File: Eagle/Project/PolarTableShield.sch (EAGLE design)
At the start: 42 parts, among them IC2 LM358D, J1 Pi Power Jack, J10 LED + Radio, J2 Header - Right angled, female, J3 Pi Connection, J5 IR Sensors, J6 Switch A + B, J7 Switch C + D, J8 Switch E + F, Q1 BC337, Q2 2N3906, Q3 BC547, Q4 2N7000, Q5 2N7000, U3 SN74HC595DR

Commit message: Layout and added frame.
Added status lights.
Matched trace lengths on the I2C bus.
Added logo.
Fixed up I2C connection on the SX1509 pins.
Added better labels and descriptions.
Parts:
- added LED1, LED2: (no value), led:LEDCHIP-LED0805
- added R13, R14: 1k, rcl:R-EU_M0805
- B1: value Connect down to Arduino -> ARDUINO_UNO_R3_SHIELDNOLABELS
- B2: value Connect up to motor shield -> ARDUINO_UNO_R3_SHIELDNOLABELS
- JP2: value Bypass Power Control -> JUMPER-SMT_2_NO_SILK
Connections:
- new net N$10: LED2.A, R14.2
- new net N$9: LED1.C, R13.1
- net !INT: now also U$1G$1.!INT; no longer U$1G$1.!RST
- net !RES: now also U$1G$1.!RST
- net 5V: now also R14.1
- net 5V_SUPPLY: now also LED1.A
- net N$6: now also R13.2
- net SCL_5V: now also LED2.C
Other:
- note added: "External 12V to 5V Buck Converter"
- note added: "Extra I2C"
- note added: "Extras"
- note added: "GPIO Expansions"
- note added: "Hard reset on button hold (5s)"
- note added: "Headers"
- note added: "Headers down to Arduino"
- note added: "Headers to Motor Shield"
- note added: "Logic Level Converter"
- note added: "Open JP3 to disable hard reset."
- note added: "Output to Raspberry Pi"
- note added: "PI Connection"
- note added: "SX1509 Headers for breakout board NOTE: 3.3V"
- note added: "Shift Register for motor settings NOTE: 5V"
- note added: "Short JP2 to disable control of Pi Power from Arduino"
- note removed: "GPIO Expander"
- note removed: "Long Press Detection (5s)"
- note removed: "PI"
- note removed: "Shift Register for motor settings"
- note removed: "Start the timer when the signal grounds"
- moved on the sheet: B1, B2, C1, C2, C4, C5, C9, D1, IC2A, J1, J10, J2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

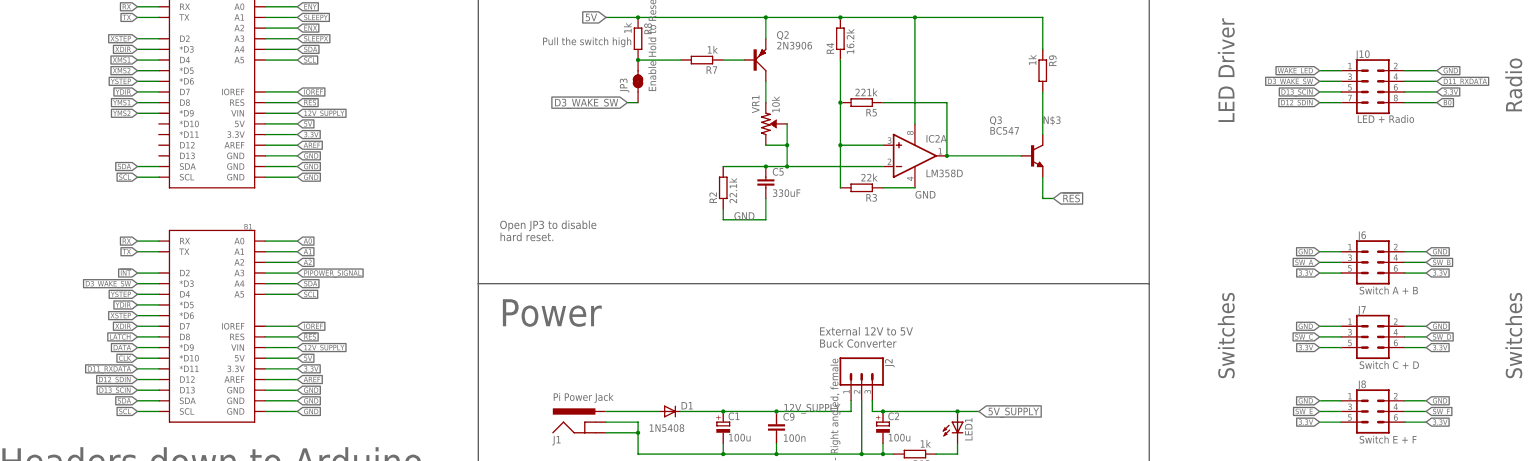
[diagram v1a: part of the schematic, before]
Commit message: Moved the LED drive connection onto hardware SPI pins.
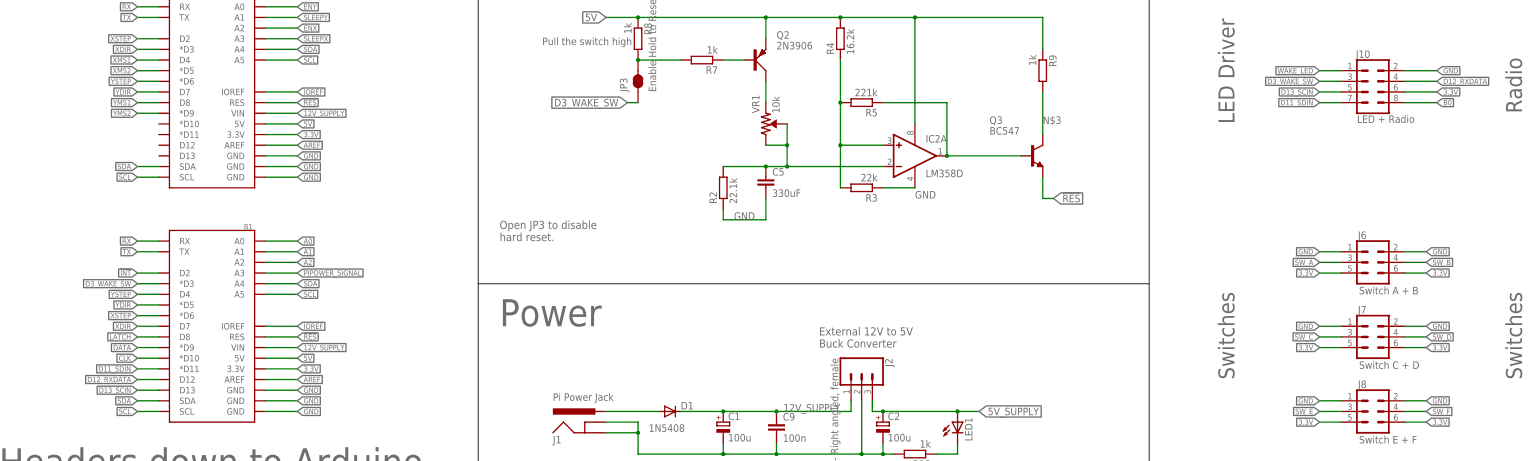
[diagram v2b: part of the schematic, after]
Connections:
- removed net D11_RXDATA: B1.*D11, J10.4
- removed net D12_SDIN: B1.D12, J10.7
- new net D11_SDIN: B1.*D11, J10.7
- new net D12_RXDATA: B1.D12, J10.4
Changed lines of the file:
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@@
 </segment>
 </net>
-<net name="D11_RXDATA" class="4">
-<segment>
-<pinref part="B1" gate="G$1" pin="*D11"/>
-<wire x1="45.72" y1="147.32" x2="40.64" y2="147.32" width="0.1524" layer="91"/>
-<label x="40.64" y="147.32" size="1.27" layer="95" rot="MR0" xref="yes"/>
-</segment>
+<net name="D12_RXDATA" class="4">
 <segment>
 <wire x1="342.9" y1="215.9" x2="350.52" y2="215.9" width="0.1524" layer="91"/>
@@
 <pinref part="J10" gate="G$1" pin="4"/>
 </segment>
-</net>
-<net name="D12_SDIN" class="4">
 <segment>
 <pinref part="B1" gate="G$1" pin="D12"/>
 <wire x1="45.72" y1="144.78" x2="40.64" y2="144.78" width="0.1524" layer="91"/>
 <label x="40.64" y="144.78" size="1.27" layer="95" rot="MR0" xref="yes"/>
-</segment>
-<segment>
-<wire x1="327.66" y1="210.82" x2="322.58" y2="210.82" width="0.1524" layer="91"/>
-<label x="322.58" y="210.82" size="1.27" layer="95" rot="MR0" xref="yes"/>
-<pinref part="J10" gate="G$1" pin="7"/>
 </segment>
 </net>
@@
 </segment>
 </net>
+<net name="D11_SDIN" class="0">
+<segment>
+<pinref part="B1" gate="G$1" pin="*D11"/>
+<wire x1="45.72" y1="147.32" x2="40.64" y2="147.32" width="0.1524" layer="91"/>
+<label x="40.64" y="147.32" size="1.27" layer="95" rot="MR0" xref="yes"/>
+</segment>
+<segment>
+<wire x1="327.66" y1="210.82" x2="322.58" y2="210.82" width="0.1524" layer="91"/>
+<label x="322.58" y="210.82" size="1.27" layer="95" rot="MR0" xref="yes"/>
+<pinref part="J10" gate="G$1" pin="7"/>
+</segment>
+</net>

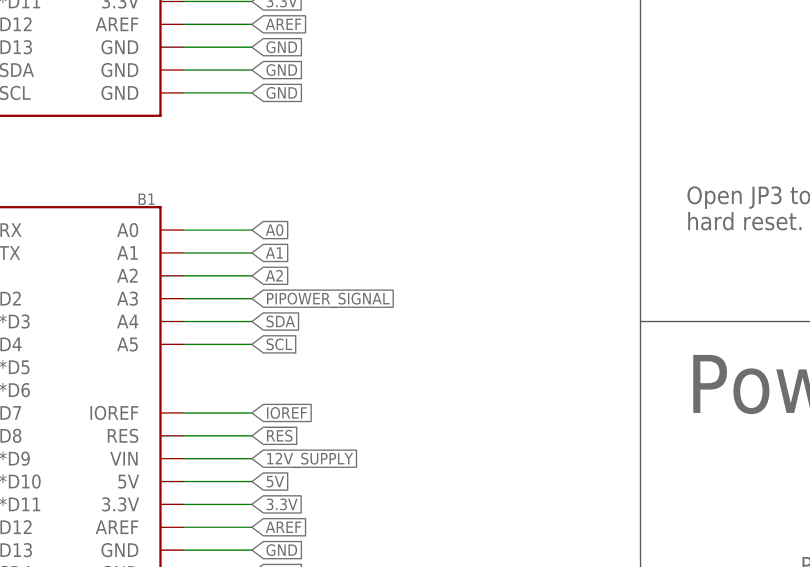
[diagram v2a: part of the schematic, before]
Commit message: Added a LED for error signals
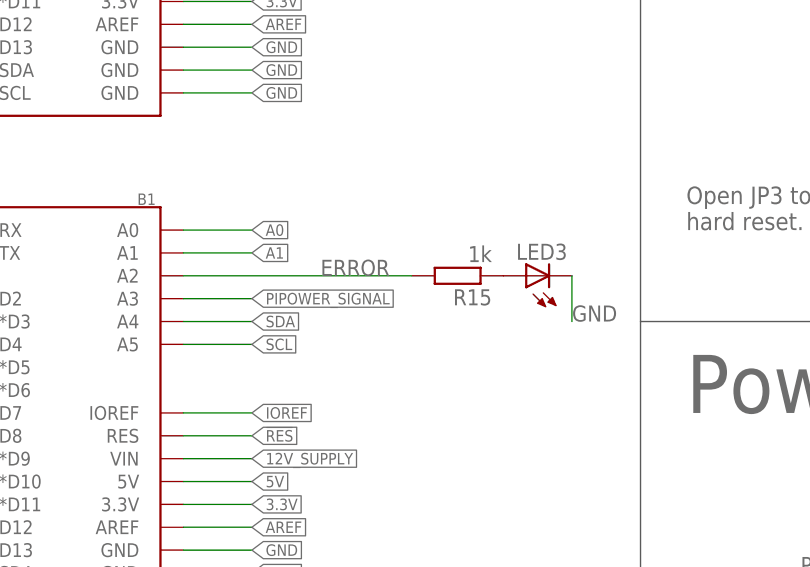
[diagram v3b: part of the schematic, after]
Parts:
- added LED3: (no value), led:LEDCHIP-LED0805
- added R15: 1k, rcl:R-EU_M0805
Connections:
- new net ERROR: B1.A2, R15.2
- new net N$11: LED3.A, R15.1
- net A2: no longer B1.A2
- net GND: now also LED3.C
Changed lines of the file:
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@@
 <part name="LED2" library="led" library_urn="urn:adsk.eagle:library:259" deviceset="LED" device="CHIP-LED0805" package3d_urn="urn:adsk.eagle:package:15818/2"/>
 <part name="R14" library="rcl" library_urn="urn:adsk.eagle:library:334" deviceset="R-EU_" device="M0805" package3d_urn="urn:adsk.eagle:package:23556/1" value="1k"/>
+<part name="LED3" library="led" library_urn="urn:adsk.eagle:library:259" deviceset="LED" device="CHIP-LED0805" package3d_urn="urn:adsk.eagle:package:15818/2"/>
+<part name="R15" library="rcl" library_urn="urn:adsk.eagle:library:334" deviceset="R-EU_" device="M0805" package3d_urn="urn:adsk.eagle:package:23556/1" value="1k"/>
 </parts>
 <sheets>
@@
 <attribute name="VALUE" x="237.998" y="41.91" size="1.778" layer="96" rot="R270"/>
 </instance>
+<instance part="LED3" gate="G$1" x="109.22" y="172.72" rot="R90">
+<attribute name="NAME" x="113.792" y="176.276" size="1.778" layer="95" rot="R180"/>
+<attribute name="VALUE" x="113.792" y="178.435" size="1.778" layer="96" rot="R180"/>
+</instance>
+<instance part="R15" gate="G$1" x="101.6" y="172.72" rot="R180">
+<attribute name="NAME" x="105.41" y="171.2214" size="1.778" layer="95" rot="R180"/>
+<attribute name="VALUE" x="105.41" y="176.022" size="1.778" layer="96" rot="R180"/>
+</instance>
 </instances>
 <busses>
@@
 <wire x1="342.9" y1="96.52" x2="347.98" y2="96.52" width="0.1524" layer="91"/>
 <label x="347.98" y="96.52" size="1.27" layer="95" xref="yes"/>
+</segment>
+<segment>
+<pinref part="LED3" gate="G$1" pin="C"/>
+<wire x1="114.3" y1="172.72" x2="114.3" y2="167.64" width="0.1524" layer="91"/>
+<label x="114.3" y="167.64" size="1.778" layer="95"/>
 </segment>
 </net>
@@
 <net name="A2" class="4">
 <segment>
-<pinref part="B1" gate="G$1" pin="A2"/>
-<wire x1="71.12" y1="172.72" x2="78.74" y2="172.72" width="0.1524" layer="91"/>
-<label x="78.74" y="172.72" size="1.27" layer="95" xref="yes"/>
-</segment>
-<segment>
 <pinref part="J5" gate="G$1" pin="6"/>
 <wire x1="342.9" y1="93.98" x2="347.98" y2="93.98" width="0.1524" layer="91"/>
@@
 </segment>
 </net>
+<net name="ERROR" class="0">
+<segment>
+<pinref part="B1" gate="G$1" pin="A2"/>
+<pinref part="R15" gate="G$1" pin="2"/>
+<wire x1="71.12" y1="172.72" x2="96.52" y2="172.72" width="0.1524" layer="91"/>
+<label x="86.36" y="172.72" size="1.778" layer="95"/>
+</segment>
+</net>
+<net name="N$11" class="0">
+<segment>
+<pinref part="R15" gate="G$1" pin="1"/>
+<pinref part="LED3" gate="G$1" pin="A"/>
+</segment>
+</net>

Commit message: Moved the relative encode switches to the Arduino
Added hardware XOR on the relative encode switches.
Combined the main switch and encoder interrupt connections.
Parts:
- removed LED3: (no value), led:LEDCHIP-LED0805
- removed R15: 1k, rcl:R-EU_M0805
- added IC1: 74AHC1G86DBV, 74xx-little-us:74AHC1G86DBV
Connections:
- removed net A0: B1.A0, J5.10
- removed net A1: B1.A1, J5.8
- removed net D3_WAKE_SW: B1.*D3, J10.3, JP3.1
- removed net ERROR: B1.A2, R15.2
- removed net N$11: LED3.A, R15.1
- removed net SW_E: J8.3, U$1G$2.P$4
- removed net SW_F: J8.4, U$1G$2.P$3
- new net A0_SW_E: B1.A0, IC1A.I0, J8.3
- new net A1_SW_F: B1.A1, IC1A.I1, J8.4
- new net A2_WAKE_SW: B1.*D3, B1.A2, IC1A.O, J10.3, JP3.1
- new net B5: J4.7, U$1G$2.P$5
- new net B6: J4.8, U$1G$2.P$6
- net B3: now also J5.8, U$1G$2.P$3; no longer J4.7, U$1G$2.P$5
- net B4: now also J5.10, U$1G$2.P$4; no longer J4.8, U$1G$2.P$6
- net GND: no longer LED3.C
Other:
- note added: "WIP: OR gate for interupts"
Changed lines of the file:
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@@
 <part name="LED2" library="led" library_urn="urn:adsk.eagle:library:259" deviceset="LED" device="CHIP-LED0805" package3d_urn="urn:adsk.eagle:package:15818/2"/>
 <part name="R14" library="rcl" library_urn="urn:adsk.eagle:library:334" deviceset="R-EU_" device="M0805" package3d_urn="urn:adsk.eagle:package:23556/1" value="1k"/>
-<part name="LED3" library="led" library_urn="urn:adsk.eagle:library:259" deviceset="LED" device="CHIP-LED0805" package3d_urn="urn:adsk.eagle:package:15818/2"/>
-<part name="R15" library="rcl" library_urn="urn:adsk.eagle:library:334" deviceset="R-EU_" device="M0805" package3d_urn="urn:adsk.eagle:package:23556/1" value="1k"/>
+<part name="IC1" library="74xx-little-us" library_urn="urn:adsk.eagle:library:87" deviceset="74*1G86" device="DBV" package3d_urn="urn:adsk.eagle:package:2406/1" technology="AHC"/>
 </parts>
 <sheets>
@@
 <text x="127" y="177.8" size="1.9304" layer="95" font="vector">Open JP3 to disable
 hard reset.</text>
+<text x="96.52" y="152.4" size="1.9304" layer="95" font="vector">WIP: OR gate for interupts</text>
 </plain>
 <instances>
@@
 <attribute name="VALUE" x="237.998" y="41.91" size="1.778" layer="96" rot="R270"/>
 </instance>
-<instance part="LED3" gate="G$1" x="109.22" y="172.72" rot="R90">
-<attribute name="NAME" x="113.792" y="176.276" size="1.778" layer="95" rot="R180"/>
-<attribute name="VALUE" x="113.792" y="178.435" size="1.778" layer="96" rot="R180"/>
-</instance>
-<instance part="R15" gate="G$1" x="101.6" y="172.72" rot="R180">
-<attribute name="NAME" x="105.41" y="171.2214" size="1.778" layer="95" rot="R180"/>
-<attribute name="VALUE" x="105.41" y="176.022" size="1.778" layer="96" rot="R180"/>
+<instance part="IC1" gate="A" x="-27.94" y="177.8">
+<attribute name="NAME" x="-35.56" y="183.515" size="1.778" layer="95"/>
+<attribute name="VALUE" x="-35.56" y="170.18" size="1.778" layer="96"/>
 </instance>
 </instances>
@@
 <wire x1="342.9" y1="96.52" x2="347.98" y2="96.52" width="0.1524" layer="91"/>
 <label x="347.98" y="96.52" size="1.27" layer="95" xref="yes"/>
-</segment>
-<segment>
-<pinref part="LED3" gate="G$1" pin="C"/>
-<wire x1="114.3" y1="172.72" x2="114.3" y2="167.64" width="0.1524" layer="91"/>
-<label x="114.3" y="167.64" size="1.778" layer="95"/>
 </segment>
 </net>
@@
 <wire x1="127" y1="30.48" x2="132.08" y2="30.48" width="0.1524" layer="91"/>
 <label x="132.08" y="30.48" size="1.27" layer="95" xref="yes"/>
-</segment>
-</net>
-<net name="SW_E" class="3">
-<segment>
-<pinref part="J8" gate="G$1" pin="3"/>
-<wire x1="327.66" y1="137.16" x2="322.58" y2="137.16" width="0.1524" layer="91"/>
-<label x="322.58" y="137.16" size="1.27" layer="95" rot="MR0" xref="yes"/>
-</segment>
-<segment>
-<pinref part="U$1" gate="G$2" pin="P$4"/>
-<wire x1="86.36" y1="35.56" x2="81.28" y2="35.56" width="0.1524" layer="91"/>
-<label x="81.28" y="35.56" size="1.27" layer="95" rot="R180" xref="yes"/>
-</segment>
-</net>
-<net name="SW_F" class="3">
-<segment>
-<pinref part="J8" gate="G$1" pin="4"/>
-<wire x1="342.9" y1="137.16" x2="347.98" y2="137.16" width="0.1524" layer="91"/>
-<label x="347.98" y="137.16" size="1.27" layer="95" xref="yes"/>
-</segment>
-<segment>
-<pinref part="U$1" gate="G$2" pin="P$3"/>
-<wire x1="86.36" y1="38.1" x2="81.28" y2="38.1" width="0.1524" layer="91"/>
-<label x="81.28" y="38.1" size="1.27" layer="95" rot="R180" xref="yes"/>
 </segment>
 </net>
@@
 </segment>
 </net>
-<net name="D3_WAKE_SW" class="4">
+<net name="A2_WAKE_SW" class="4">
 <segment>
 <label x="322.58" y="215.9" size="1.27" layer="95" rot="MR0" xref="yes"/>
@@
 </segment>
 <segment>
+<label x="78.74" y="172.72" size="1.27" layer="95" rot="MR180" xref="yes"/>
+<pinref part="B1" gate="G$1" pin="A2"/>
+<wire x1="78.74" y1="172.72" x2="71.12" y2="172.72" width="0.1524" layer="91"/>
+</segment>
+<segment>
+<wire x1="-50.8" y1="165.1" x2="-10.16" y2="165.1" width="0.1524" layer="91"/>
+<wire x1="-10.16" y1="165.1" x2="-10.16" y2="175.26" width="0.1524" layer="91"/>
+<label x="-55.88" y="165.1" size="1.778" layer="95"/>
 <pinref part="B1" gate="G$1" pin="*D3"/>
-<wire x1="45.72" y1="167.64" x2="40.64" y2="167.64" width="0.1524" layer="91"/>
-<label x="40.64" y="167.64" size="1.27" layer="95" rot="MR0" xref="yes"/>
+<wire x1="25.4" y1="175.26" x2="25.4" y2="167.64" width="0.1524" layer="91"/>
+<wire x1="25.4" y1="167.64" x2="45.72" y2="167.64" width="0.1524" layer="91"/>
+<pinref part="IC1" gate="A" pin="O"/>
+<wire x1="-15.24" y1="177.8" x2="-10.16" y2="177.8" width="0.1524" layer="91"/>
+<wire x1="25.4" y1="175.26" x2="-10.16" y2="175.26" width="0.1524" layer="91"/>
+<wire x1="-10.16" y1="175.26" x2="-10.16" y2="177.8" width="0.1524" layer="91"/>
+<junction x="-10.16" y="175.26"/>
 </segment>
 </net>
@@
 </segment>
 </net>
-<net name="B4" class="3">
+<net name="B6" class="3">
 <segment>
 <pinref part="U$1" gate="G$2" pin="P$6"/>
@@
 </segment>
 </net>
-<net name="B3" class="3">
+<net name="B5" class="3">
 <segment>
 <pinref part="U$1" gate="G$2" pin="P$5"/>
@@
 </segment>
 </net>
-<net name="A0" class="4">
+<net name="A0_SW_E" class="4">
 <segment>
 <pinref part="B1" gate="G$1" pin="A0"/>
@@
 </segment>
 <segment>
-<pinref part="J5" gate="G$1" pin="10"/>
-<wire x1="342.9" y1="88.9" x2="347.98" y2="88.9" width="0.1524" layer="91"/>
-<label x="347.98" y="88.9" size="1.27" layer="95" xref="yes"/>
-</segment>
-</net>
-<net name="A1" class="4">
+<pinref part="J8" gate="G$1" pin="3"/>
+<wire x1="327.66" y1="137.16" x2="322.58" y2="137.16" width="0.1524" layer="91"/>
+<label x="322.58" y="137.16" size="1.27" layer="95" rot="MR0" xref="yes"/>
+</segment>
+<segment>
+<pinref part="IC1" gate="A" pin="I0"/>
+<wire x1="-40.64" y1="180.34" x2="-50.8" y2="180.34" width="0.1524" layer="91"/>
+<label x="-55.88" y="180.34" size="1.778" layer="95"/>
+</segment>
+</net>
+<net name="A1_SW_F" class="4">
 <segment>
 <pinref part="B1" gate="G$1" pin="A1"/>
@@
 </segment>
 <segment>
-<pinref part="J5" gate="G$1" pin="8"/>
-<wire x1="342.9" y1="91.44" x2="347.98" y2="91.44" width="0.1524" layer="91"/>
-<label x="347.98" y="91.44" size="1.27" layer="95" xref="yes"/>
+<pinref part="J8" gate="G$1" pin="4"/>
+<wire x1="342.9" y1="137.16" x2="347.98" y2="137.16" width="0.1524" layer="91"/>
+<label x="347.98" y="137.16" size="1.27" layer="95" xref="yes"/>
+</segment>
+<segment>
+<pinref part="IC1" gate="A" pin="I1"/>
+<wire x1="-40.64" y1="175.26" x2="-50.8" y2="175.26" width="0.1524" layer="91"/>
+<label x="-55.88" y="175.26" size="1.778" layer="95"/>
 </segment>
 </net>
@@
 </segment>
 </net>
-<net name="ERROR" class="0">
-<segment>
-<pinref part="B1" gate="G$1" pin="A2"/>
-<pinref part="R15" gate="G$1" pin="2"/>
-<wire x1="71.12" y1="172.72" x2="96.52" y2="172.72" width="0.1524" layer="91"/>
-<label x="86.36" y="172.72" size="1.778" layer="95"/>
-</segment>
-</net>
-<net name="N$11" class="0">
-<segment>
-<pinref part="R15" gate="G$1" pin="1"/>
-<pinref part="LED3" gate="G$1" pin="A"/>
-</segment>
-</net>
+<net name="B3" class="4">
+<segment>
+<pinref part="U$1" gate="G$2" pin="P$3"/>
+<wire x1="86.36" y1="38.1" x2="81.28" y2="38.1" width="0.1524" layer="91"/>
+<label x="81.28" y="38.1" size="1.27" layer="95" rot="R180" xref="yes"/>
+</segment>
+<segment>
+<pinref part="J5" gate="G$1" pin="8"/>
+<wire x1="342.9" y1="91.44" x2="347.98" y2="91.44" width="0.1524" layer="91"/>
+<label x="347.98" y="91.44" size="1.27" layer="95" xref="yes"/>
+</segment>
+</net>
+<net name="B4" class="4">
+<segment>
+<pinref part="U$1" gate="G$2" pin="P$4"/>
+<wire x1="86.36" y1="35.56" x2="81.28" y2="35.56" width="0.1524" layer="91"/>
+<label x="81.28" y="35.56" size="1.27" layer="95" rot="R180" xref="yes"/>
+</segment>
+<segment>
+<pinref part="J5" gate="G$1" pin="10"/>
+<wire x1="342.9" y1="88.9" x2="347.98" y2="88.9" width="0.1524" layer="91"/>
+<label x="347.98" y="88.9" size="1.27" layer="95" xref="yes"/>
+</segment>
+</net>
